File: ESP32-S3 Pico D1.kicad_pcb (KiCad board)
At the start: 6 copper layers, 31 x 30.5 mm, 70 parts, among them CN501 GT-USB-7014D, SW601 SPST-NO, SW602 SPST-NO, U401 ESP32-S3-PICO-1-N8R2, U501 TPS2121, U502 TPSM82903

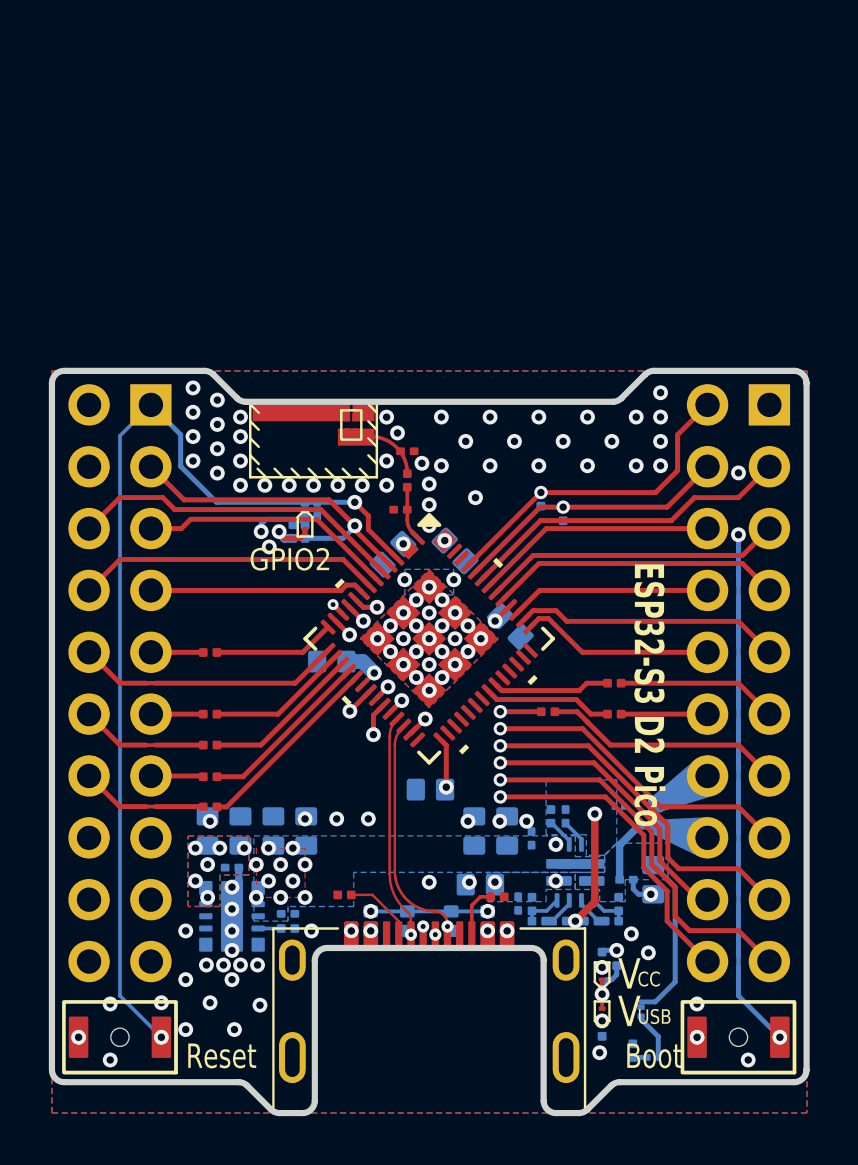
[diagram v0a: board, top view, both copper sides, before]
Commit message: added new ESP32-S3 D1 Pico symbol and footprint
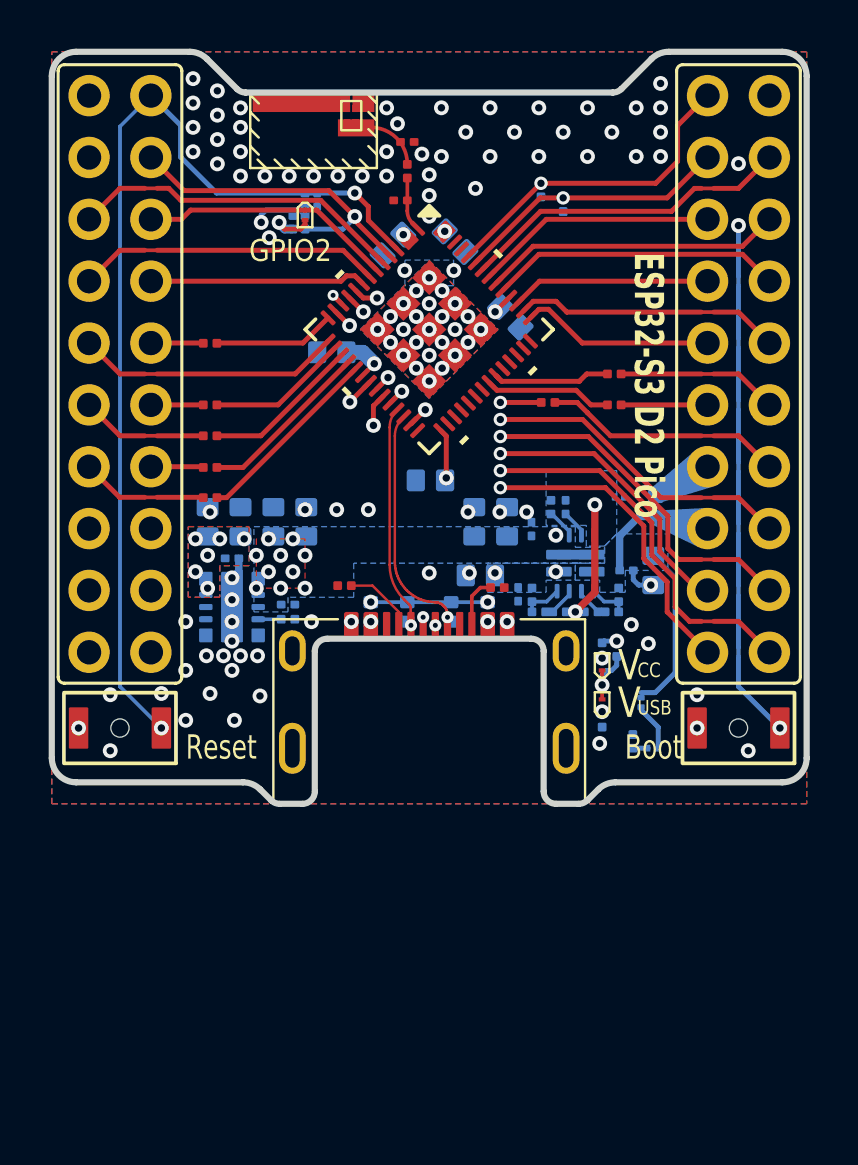
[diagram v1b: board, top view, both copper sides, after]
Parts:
- removed H201, H202: ESP_Header, My Connectors:PinHeader_2x10_P2.54mm_Vertical_THT_BottomMount_TopReference
- added U201: ~, Personal_FootprintLibrary:ESP32-S3_D1_Pico, F.Cu at (150.0, 100.0)
- moved C401 12.7 mm to (148.5, 93.4)
- moved C402 12.7 mm to (150.1, 103.1)
- moved C403 12.7 mm to (153.3, 96.4)
- moved C404 12.7 mm to (151.1, 93.3)
- moved C405 12.7 mm to (146.0, 97.8)
- moved C406 12.7 mm to (148.8, 91.6)
- moved C407 12.7 mm to (149.1, 89.2)
- moved C501 12.7 mm to (159.2, 106.8)
- moved C502 12.7 mm to (158.1, 106.8)
- moved C503 12.7 mm to (152.1, 107.0)
- moved C504 12.7 mm to (153.7, 107.8)
- moved C505 12.7 mm to (155.6, 104.2)
- moved C506 12.7 mm to (154.2, 105.1)
- moved C507 12.7 mm to (153.2, 104.8)
- moved C508 12.7 mm to (151.8, 104.8)
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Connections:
- net /ESP32-S3 Board/EN/~{Reset} renamed /EN/~{Reset}
- net /ESP32-S3 Board/ESP32-S3-PICO-1/GPIO09 renamed /ESP32-S3-PICO-1/GPIO09
- net /ESP32-S3 Board/ESP32-S3-PICO-1/GPIO11 renamed /ESP32-S3-PICO-1/GPIO11
- net /ESP32-S3 Board/ESP32-S3-PICO-1/GPIO12 renamed /ESP32-S3-PICO-1/GPIO12
- net /ESP32-S3 Board/ESP32-S3-PICO-1/GPIO13 renamed /ESP32-S3-PICO-1/GPIO13
- net /ESP32-S3 Board/ESP32-S3-PICO-1/GPIO14 renamed /ESP32-S3-PICO-1/GPIO14
- net /ESP32-S3 Board/ESP32-S3-PICO-1/GPIO21 renamed /ESP32-S3-PICO-1/GPIO21
- net /ESP32-S3 Board/ESP32-S3-PICO-1/RF_Feed renamed /ESP32-S3-PICO-1/RF_Feed
- net /ESP32-S3 Board/ESP32-S3-PICO-1/RF_In renamed /ESP32-S3-PICO-1/RF_In
- net /ESP32-S3 Board/ESP32-S3-PICO-1/USB_D+ renamed /ESP32-S3-PICO-1/USB_D+
- net /ESP32-S3 Board/ESP32-S3-PICO-1/USB_D- renamed /ESP32-S3-PICO-1/USB_D-
- net /ESP32-S3 Board/IO00 renamed /IO00
- net /ESP32-S3 Board/IO02 renamed /IO02
- net /ESP32-S3 Board/IO45 renamed /IO45
- net /ESP32-S3 Board/IO46 renamed /IO46
- net /ESP32-S3 Board/USB_Power_Interface/CC1 renamed /USB_Power_Interface/CC1
- net /ESP32-S3 Board/USB_Power_Interface/CC2 renamed /USB_Power_Interface/CC2
- net /ESP32-S3 Board/USB_Power_Interface/CP2 renamed /USB_Power_Interface/CP2
- net /ESP32-S3 Board/USB_Power_Interface/GND1 renamed /USB_Power_Interface/GND1
- net /ESP32-S3 Board/USB_Power_Interface/ILM renamed /USB_Power_Interface/ILM
- net /ESP32-S3 Board/USB_Power_Interface/OV1 renamed /USB_Power_Interface/OV1
- net /ESP32-S3 Board/USB_Power_Interface/OV2 renamed /USB_Power_Interface/OV2
- net /ESP32-S3 Board/USB_Power_Interface/PR1 renamed /USB_Power_Interface/PR1
- net /ESP32-S3 Board/USB_Power_Interface/Pwr Src Ind renamed /USB_Power_Interface/Pwr Src Ind
- net /ESP32-S3 Board/USB_Power_Interface/SCONFd renamed /USB_Power_Interface/SCONFd
- net /ESP32-S3 Board/USB_Power_Interface/SS renamed /USB_Power_Interface/SS
- net /ESP32-S3 Board/User Interface/LED1_H renamed /User Interface/LED1_H
- net /ESP32-S3 Board/User Interface/LED2_H renamed /User Interface/LED2_H
- net /ESP32-S3 Board/User Interface/LED3_L renamed /User Interface/LED3_L
- net /ESP32-S3 Board/User Interface/LED4_H renamed /User Interface/LED4_H
- net /ESP32-S3 Board/User Interface/LED4_L renamed /User Interface/LED4_L
- R401 pad 2: /ESP32-S3 Board/IO09 -> /IO09
- R402 pad 2: /ESP32-S3 Board/IO11 -> /IO11
- R403 pad 2: /ESP32-S3 Board/IO12 -> /IO12
- R404 pad 2: /ESP32-S3 Board/IO13 -> /IO13
- R405 pad 2: /ESP32-S3 Board/IO14 -> /IO14
- R406 pad 2: /ESP32-S3 Board/IO21 -> /IO21
- R407 pad 1: /ESP32-S3 Board/IO47 -> /IO47
- R408 pad 1: /ESP32-S3 Board/IO48 -> /IO48
- U401 pad 10: /ESP32-S3 Board/IO05 -> /IO05
- U401 pad 11: /ESP32-S3 Board/IO06 -> /IO06
- U401 pad 12: /ESP32-S3 Board/IO07 -> /IO07
- U401 pad 13: /ESP32-S3 Board/IO08 -> /IO08
- U401 pad 15: /ESP32-S3 Board/IO10 -> /IO10
- U401 pad 21: /ESP32-S3 Board/IO15 -> /IO15
- U401 pad 22: /ESP32-S3 Board/IO16 -> /IO16
- U401 pad 23: /ESP32-S3 Board/IO17 -> /IO17
- U401 pad 24: /ESP32-S3 Board/IO18 -> /IO18
- U401 pad 43: /ESP32-S3 Board/IO38 -> /IO38
- U401 pad 44: /ESP32-S3 Board/IO39 -> /IO39
- U401 pad 45: /ESP32-S3 Board/IO40 -> /IO40
- U401 pad 47: /ESP32-S3 Board/IO41 -> /IO41
- U401 pad 48: /ESP32-S3 Board/IO42 -> /IO42
- U401 pad 49: /ESP32-S3 Board/IO43 -> /IO43
- U401 pad 50: /ESP32-S3 Board/IO44 -> /IO44
- U401 pad 6: /ESP32-S3 Board/IO01 -> /IO01
- U401 pad 8: /ESP32-S3 Board/IO03 -> /IO03
- U401 pad 9: /ESP32-S3 Board/IO04 -> /IO04
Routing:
- net /ESP32-S3 Board/IO08: track 25.6 -> 0.00 mm, vias 2 -> 0
- net /IO08: track 0.00 -> 25.6 mm, vias 0 -> 2
- net /IO15: track 0.00 -> 24.4 mm, vias 0 -> 2
- net /ESP32-S3 Board/IO15: track 24.4 -> 0.00 mm, vias 2 -> 0
- net /ESP32-S3 Board/IO05: track 24.2 -> 0.00 mm, vias 1 -> 0
- net /IO05: track 0.00 -> 24.2 mm, vias 0 -> 1
- net /IO07: track 0.00 -> 22.5 mm, vias 0 -> 1
- net /ESP32-S3 Board/IO07: track 22.5 -> 0.00 mm, vias 1 -> 0
- net /IO16: track 0.00 -> 21.6 mm, vias 0 -> 2
- net /ESP32-S3 Board/IO16: track 21.6 -> 0.00 mm, vias 2 -> 0
- net /IO17: track 0.00 -> 18.8 mm, vias 0 -> 2
- net /ESP32-S3 Board/IO17: track 18.8 -> 0.00 mm, vias 2 -> 0
- net /IO18: track 0.00 -> 18.6 mm, vias 0 -> 2
- net /ESP32-S3 Board/IO18: track 18.6 -> 0.00 mm, vias 2 -> 0
- net /IO06: track 0.00 -> 18.4 mm, vias 0 -> 1
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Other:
- board size 31 x 30.5 mm -> 31 x 30.9 mm

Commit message: Update ESP32-S3 Pico D1-Main.kicad_sch, ESP32-S3 Pico D1.kicad_pcb, ESP32-S3 Pico D1.kicad_prl, and 7 more files
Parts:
- D506, D601: footprint Personal_FootprintLibrary:DSN0603-2 -> My Package_Leadless:DFN0603-2
- R401, R402, R403, R404, R405, R406, R407, R408, R409, R410, R501, R502, R601, R602, R603, R604, R605, R606, R607: footprint My Resistors:R_0201_Dense -> My Resistors:R_0201_Nominal
- moved R602 1.05 mm to (145.4, 93.4)
- moved R603 0.93 mm to (144.4, 93.4)
- moved C601 0.85 mm to (146.2, 91.6)
- moved R601 0.54 mm to (145.4, 91.8)
- moved R607 0.21 mm to (158.2, 113.8)
- moved R604 0.20 mm to (157.9, 110.0)
- moved R606 0.20 mm to (156.9, 110.0)
- moved R409 0.12 mm to (155.6, 91.8)
- moved R405 0.11 mm to (141.0, 103.7)
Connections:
- net +3V3 renamed /ESP32-S3 Pico D1-Main/+3V3
- net +5V_{EXT} renamed /+5V_{EXT}
- net +5V_{FUSED} renamed /ESP32-S3 Pico D1-Main/+5V_{FUSED}
- net +V_{BUS} renamed /ESP32-S3 Pico D1-Main/USB_Power_Interface/+V_{BUS}
- net /EN/~{Reset} renamed /ESP32-S3 Pico D1-Main/EN/~{Reset}
- net /ESP32-S3-PICO-1/GPIO09 renamed /ESP32-S3 Pico D1-Main/ESP32-S3-PICO-1/GPIO09
- net /ESP32-S3-PICO-1/GPIO11 renamed /ESP32-S3 Pico D1-Main/ESP32-S3-PICO-1/GPIO11
- net /ESP32-S3-PICO-1/GPIO12 renamed /ESP32-S3 Pico D1-Main/ESP32-S3-PICO-1/GPIO12
- net /ESP32-S3-PICO-1/GPIO13 renamed /ESP32-S3 Pico D1-Main/ESP32-S3-PICO-1/GPIO13
- net /ESP32-S3-PICO-1/GPIO14 renamed /ESP32-S3 Pico D1-Main/ESP32-S3-PICO-1/GPIO14
- net /ESP32-S3-PICO-1/GPIO21 renamed /ESP32-S3 Pico D1-Main/ESP32-S3-PICO-1/GPIO21
- net /ESP32-S3-PICO-1/RF_Feed renamed /ESP32-S3 Pico D1-Main/ESP32-S3-PICO-1/RF_Feed
- net /ESP32-S3-PICO-1/RF_In renamed /ESP32-S3 Pico D1-Main/ESP32-S3-PICO-1/RF_In
- net /ESP32-S3-PICO-1/USB_D+ renamed /ESP32-S3 Pico D1-Main/ESP32-S3-PICO-1/USB_D+
- net /ESP32-S3-PICO-1/USB_D- renamed /ESP32-S3 Pico D1-Main/ESP32-S3-PICO-1/USB_D-
- net /IO00 renamed /ESP32-S3 Pico D1-Main/IO00
- net /IO01 renamed /ESP32-S3 Pico D1-Main/IO01
- net /IO02 renamed /ESP32-S3 Pico D1-Main/IO02
- net /IO03 renamed /ESP32-S3 Pico D1-Main/IO03
- net /IO04 renamed /ESP32-S3 Pico D1-Main/IO04
- net /IO05 renamed /ESP32-S3 Pico D1-Main/IO05
- net /IO06 renamed /ESP32-S3 Pico D1-Main/IO06
- net /IO07 renamed /ESP32-S3 Pico D1-Main/IO07
- net /IO08 renamed /ESP32-S3 Pico D1-Main/IO08
- net /IO09 renamed /ESP32-S3 Pico D1-Main/IO09
- net /IO10 renamed /ESP32-S3 Pico D1-Main/IO10
- net /IO11 renamed /ESP32-S3 Pico D1-Main/IO11
- net /IO12 renamed /ESP32-S3 Pico D1-Main/IO12
- net /IO13 renamed /ESP32-S3 Pico D1-Main/IO13
- net /IO14 renamed /ESP32-S3 Pico D1-Main/IO14
- net /IO15 renamed /ESP32-S3 Pico D1-Main/IO15
- net /IO16 renamed /ESP32-S3 Pico D1-Main/IO16
- net /IO17 renamed /ESP32-S3 Pico D1-Main/IO17
- net /IO18 renamed /ESP32-S3 Pico D1-Main/IO18
- net /IO21 renamed /ESP32-S3 Pico D1-Main/IO21
- net /IO38 renamed /ESP32-S3 Pico D1-Main/IO38
- net /IO39 renamed /ESP32-S3 Pico D1-Main/IO39
- net /IO40 renamed /ESP32-S3 Pico D1-Main/IO40
- net /IO41 renamed /ESP32-S3 Pico D1-Main/IO41
- net /IO42 renamed /ESP32-S3 Pico D1-Main/IO42
- net /IO43 renamed /ESP32-S3 Pico D1-Main/IO43
- net /IO44 renamed /ESP32-S3 Pico D1-Main/IO44
- net /IO45 renamed /ESP32-S3 Pico D1-Main/IO45
- net /IO46 renamed /ESP32-S3 Pico D1-Main/IO46
- net /IO47 renamed /ESP32-S3 Pico D1-Main/IO47
- net /IO48 renamed /ESP32-S3 Pico D1-Main/IO48
- net /USB_Power_Interface/CC1 renamed /ESP32-S3 Pico D1-Main/USB_Power_Interface/CC1
- net /USB_Power_Interface/CC2 renamed /ESP32-S3 Pico D1-Main/USB_Power_Interface/CC2
- net /USB_Power_Interface/CP2 renamed /ESP32-S3 Pico D1-Main/USB_Power_Interface/CP2
- net /USB_Power_Interface/GND1 renamed /ESP32-S3 Pico D1-Main/USB_Power_Interface/GND1
- net /USB_Power_Interface/ILM renamed /ESP32-S3 Pico D1-Main/USB_Power_Interface/ILM
- net /USB_Power_Interface/OV1 renamed /ESP32-S3 Pico D1-Main/USB_Power_Interface/OV1
- net /USB_Power_Interface/OV2 renamed /ESP32-S3 Pico D1-Main/USB_Power_Interface/OV2
- net /USB_Power_Interface/PR1 renamed /ESP32-S3 Pico D1-Main/USB_Power_Interface/PR1
- net /USB_Power_Interface/Pwr Src Ind renamed /ESP32-S3 Pico D1-Main/USB_Power_Interface/Pwr Src Ind
- net /USB_Power_Interface/SCONFd renamed /ESP32-S3 Pico D1-Main/USB_Power_Interface/SCONFd
- net /USB_Power_Interface/SS renamed /ESP32-S3 Pico D1-Main/USB_Power_Interface/SS
- net /User Interface/LED1_H renamed /ESP32-S3 Pico D1-Main/User Interface/LED1_H
- net /User Interface/LED2_H renamed /ESP32-S3 Pico D1-Main/User Interface/LED2_H
- net /User Interface/LED3_L renamed /ESP32-S3 Pico D1-Main/User Interface/LED3_L
- net /User Interface/LED4_H renamed /ESP32-S3 Pico D1-Main/User Interface/LED4_H
- net /User Interface/LED4_L renamed /ESP32-S3 Pico D1-Main/User Interface/LED4_L
- net GND renamed /GND
- net GND0 renamed /GND0
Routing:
- net /ESP32-S3 Pico D1-Main/User Interface/LED1_H: track 0.00 -> 2.82 mm
- net /ESP32-S3 Pico D1-Main/User Interface/LED2_H: track 2.18 -> 3.17 mm
- net /ESP32-S3 Pico D1-Main/IO00: track 55.3 -> 55.9 mm
- net /ESP32-S3 Pico D1-Main/+3V3: track 19.0 -> 19.6 mm
- added copper zone on B.Cu, net /ESP32-S3 Pico D1-Main/USB_Power_Interface/CP2
- added copper zone on B.Cu, net /ESP32-S3 Pico D1-Main/USB_Power_Interface/PR1
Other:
- board text added: "ESP32-S3 D1 Pico"
- board text added: "JLCJLCJLCJLC"
- board text added: "RHK ESP32-S3 D1 Pico"
- board text removed: "ESP32-S3 D2 Pico"
- board text removed: "RHK ESP32-S3 D2 Pico"
